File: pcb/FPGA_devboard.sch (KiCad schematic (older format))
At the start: 0 parts

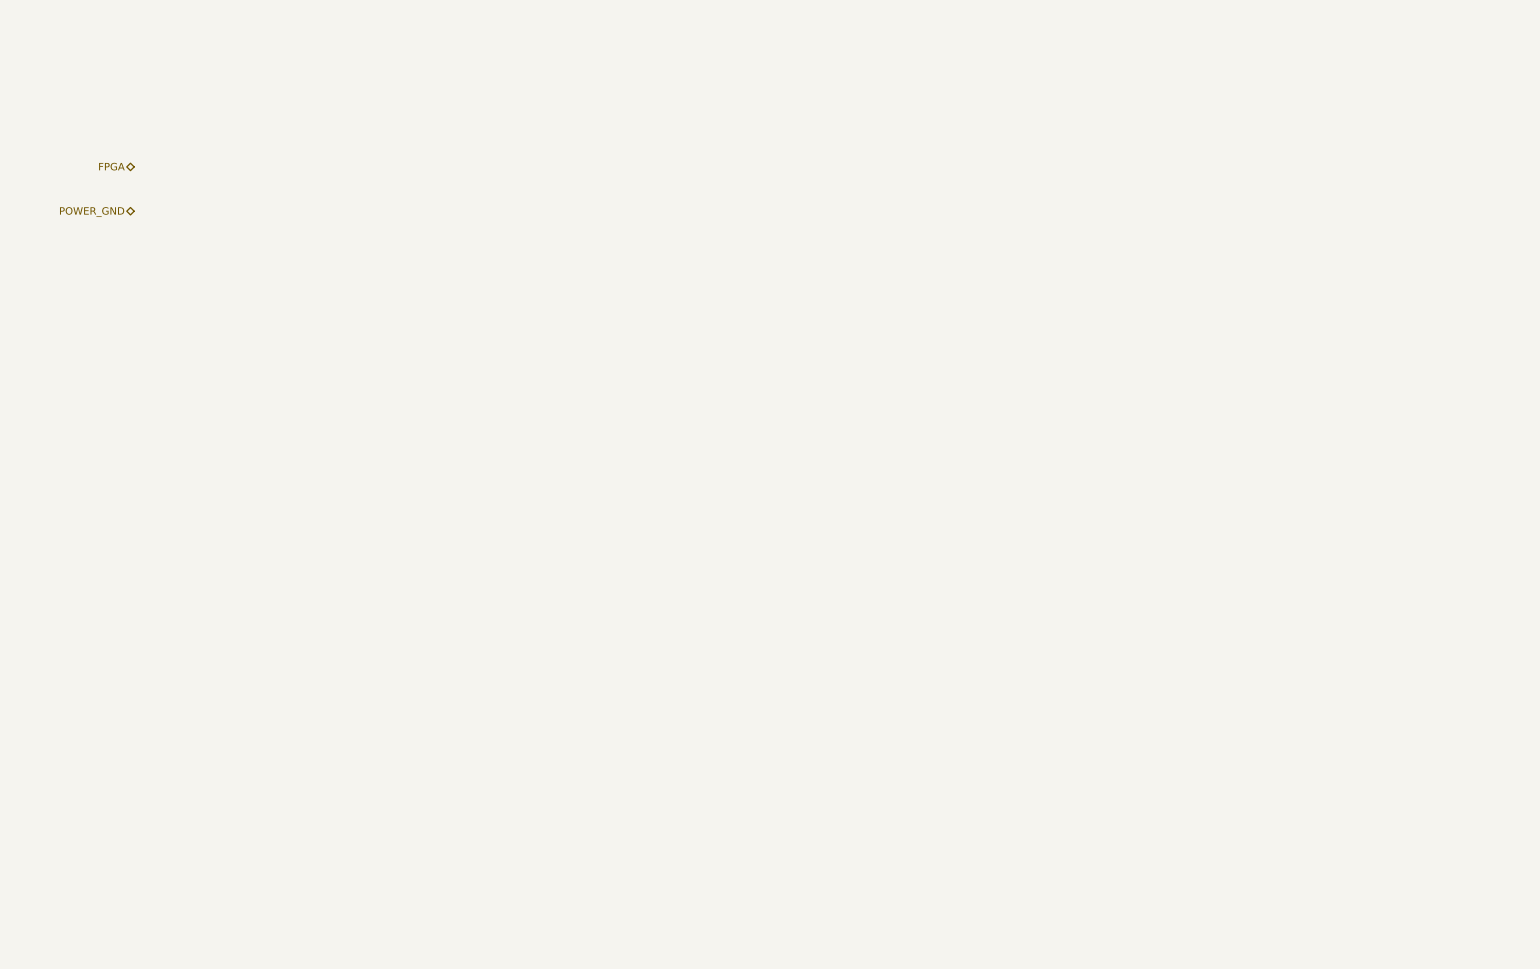
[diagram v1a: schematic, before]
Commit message: AC7020 schlib and sch list updated
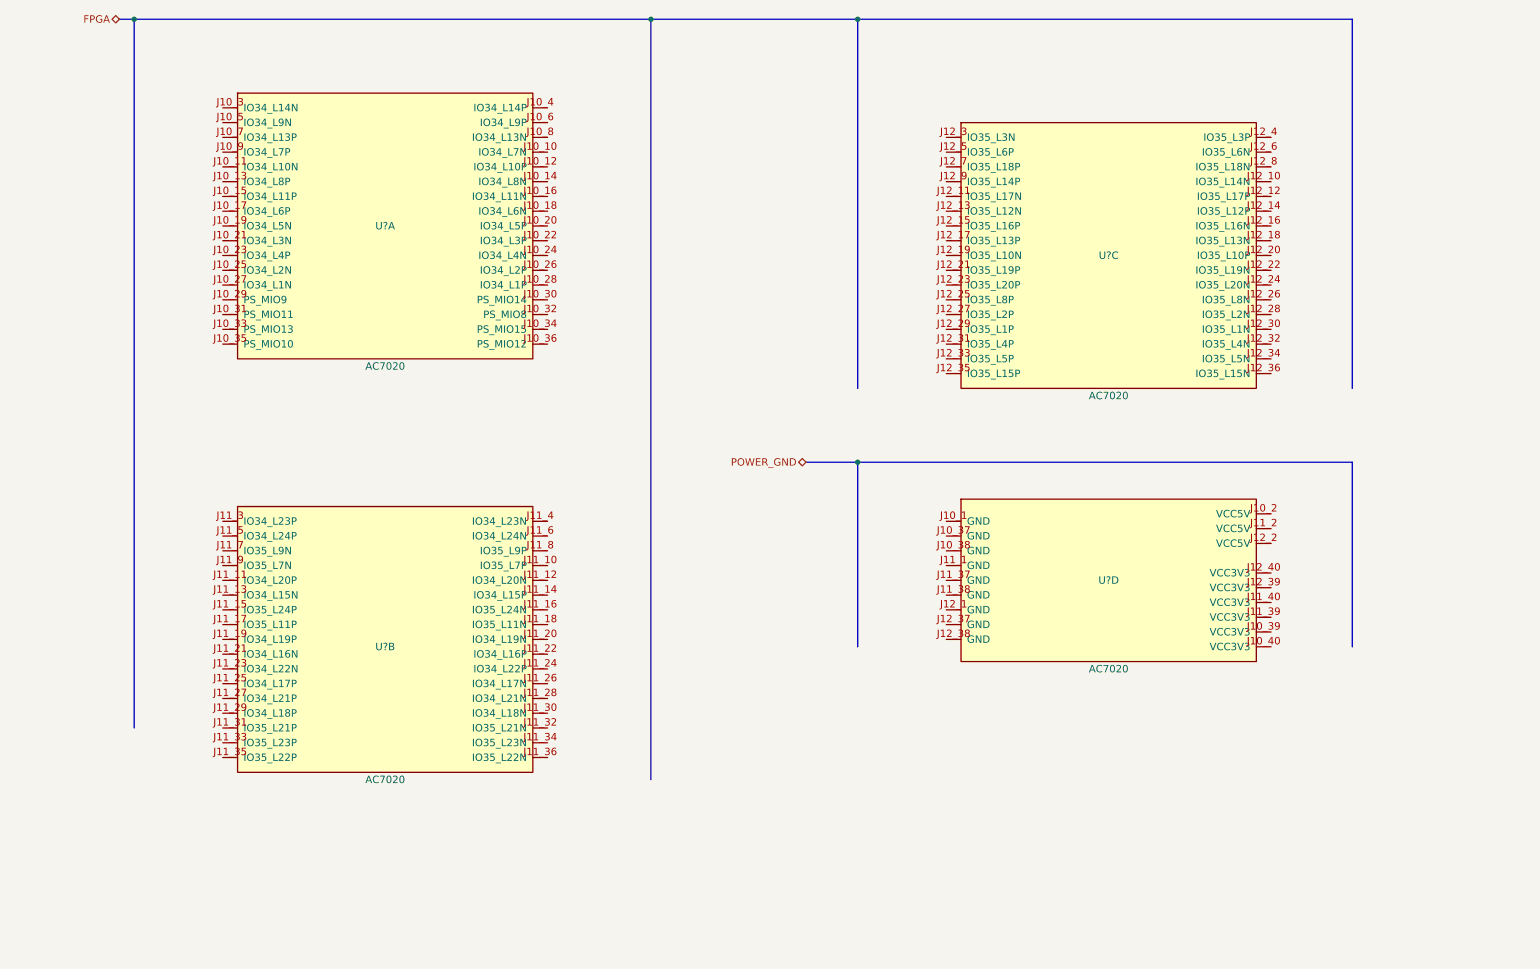
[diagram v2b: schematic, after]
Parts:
- added U? (x4): AC7020, symbol WM1200:AC7020
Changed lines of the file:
@@
 Comment4 ""
 $EndDescr
-Text HLabel 1500 2000 0    50   BiDi ~ 0
+Text HLabel 1400 1000 0    50   BiDi ~ 0
 FPGA
-Text HLabel 1500 2300 0    50   BiDi ~ 0
+Text HLabel 6050 4000 0    50   BiDi ~ 0
 POWER_GND
+$Comp
+L WM1200:AC7020 U?
+U 1 1 5EB9A3F4
+P 3200 3300
+F 0 "U?" H 3200 4200 50  0000 C CNN
+F 1 "AC7020" H 3200 3250 50  0000 C CNN
+F 2 "" H 3200 3300 50  0001 C CNN
+F 3 "" H 3200 3300 50  0001 C CNN
+	1    3200 3300
+	1    0    0    -1
+$EndComp
+$Comp
+L WM1200:AC7020 U?
+U 2 1 5EBA0B64
+P 3200 6100
+F 0 "U?" H 3200 6950 50  0000 C CNN
+F 1 "AC7020" H 3200 6050 50  0000 C CNN
+F 2 "" H 3200 6100 50  0001 C CNN
+F 3 "" H 3200 6100 50  0001 C CNN
+	2    3200 6100
+	1    0    0    -1
+$EndComp
+$Comp
+L WM1200:AC7020 U?
+U 3 1 5EBA7395
+P 8100 3500
+F 0 "U?" H 8100 4400 50  0000 C CNN
+F 1 "AC7020" H 8100 3450 50  0000 C CNN
+F 2 "" H 8100 3500 50  0001 C CNN
+F 3 "" H 8100 3500 50  0001 C CNN
+	3    8100 3500
+	1    0    0    -1
+$EndComp
+Wire Bus Line
+	1400 1000 1500 1000
+Wire Bus Line
+	1500 1000 1500 5800
+Wire Bus Line
+	1500 1000 5000 1000
+Wire Bus Line
+	5000 1000 5000 6150
+Connection ~ 1500 1000
+Wire Bus Line
+	5000 1000 6400 1000
+Wire Bus Line
+	6400 1000 6400 3500
+Connection ~ 5000 1000
+Wire Bus Line
+	6400 1000 9750 1000
+Wire Bus Line
+	9750 1000 9750 3500
+Connection ~ 6400 1000
+$Comp
+L WM1200:AC7020 U?
+U 4 1 5EBCCB73
+P 8100 5350
+F 0 "U?" H 8100 5900 50  0000 C CNN
+F 1 "AC7020" H 8100 5300 50  0000 C CNN
+F 2 "" H 8100 5350 50  0001 C CNN
+F 3 "" H 8100 5350 50  0001 C CNN
+	4    8100 5350
+	1    0    0    -1
+$EndComp
+Wire Bus Line
+	6050 4000 6400 4000
+Wire Bus Line
+	6400 4000 6400 5250
+Wire Bus Line
+	6400 4000 9750 4000
+Wire Bus Line
+	9750 4000 9750 5250
+Connection ~ 6400 4000
 $EndSCHEMATC

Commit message: Some work done on the whole project
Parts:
- gave numbers to parts that had none: 1
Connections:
- net FPGA_A17: now reaches X3.J10_10 (IO34_L7N)
- net FPGA_A4: now reaches X3.J10_11 (IO34_L10N)
- net FPGA_A18: now reaches X3.J10_12 (IO34_L10P)
- net FPGA_A5: now reaches X3.J10_13 (IO34_L8P)
- net FPGA_A19: now reaches X3.J10_14 (IO34_L8N)
- net FPGA_A6: now reaches X3.J10_15 (IO34_L11P)
- net FPGA_A20: now reaches X3.J10_16 (IO34_L11N)
- net FPGA_A7: now reaches X3.J10_17 (IO34_L6P)
- net FPGA_A21: now reaches X3.J10_18 (IO34_L6N)
- net FPGA_A8: now reaches X3.J10_19 (IO34_L5N)
- net FPGA_A22: now reaches X3.J10_20 (IO34_L5P)
- net FPGA_A9: now reaches X3.J10_21 (IO34_L3N)
- net FPGA_A23: now reaches X3.J10_22 (IO34_L3P)
- net FPGA_A10: now reaches X3.J10_23 (IO34_L4P)
- net A_BUFF_DIR: now reaches X3.J10_24 (IO34_L4N)
- net FPGA_A11: now reaches X3.J10_25 (IO34_L2N)
- net _A_BUFF_OE: now reaches X3.J10_26 (IO34_L2P)
- net FPGA_A12: now reaches X3.J10_27 (IO34_L1N)
- net FPGA_A0: now reaches X3.J10_3 (IO34_L14N)
- net FPGA_A13: now reaches X3.J10_4 (IO34_L14P)
- net FPGA_A1: now reaches X3.J10_5 (IO34_L9N)
- net FPGA_A14: now reaches X3.J10_6 (IO34_L9P)
- net FPGA_A2: now reaches X3.J10_7 (IO34_L13P)
- net FPGA_A15: now reaches X3.J10_8 (IO34_L13N)
- net FPGA_A3: now reaches X3.J10_9 (IO34_L7P)
- net FPGA_: now reaches X3.J11_10 (IO35_L7P)
- net FPGA_: now also X3.J11_11 (IO34_L20P), X3.J11_12 (IO34_L20N), X3.J11_13 (IO34_L15N), X3.J11_14 (IO34_L15P), X3.J11_15 (IO35_L24P), X3.J11_16 (IO35_L24N), X3.J11_17 (IO35_L11P), X3.J11_18 (IO35_L11N), X3.J11_19 (IO34_L19P), X3.J11_20 (IO34_L19N), X3.J11_21 (IO34_L16N), X3.J11_22 (IO34_L16P), X3.J11_23 (IO34_L22N), X3.J11_24 (IO34_L22P), X3.J11_25 (IO34_L17P), X3.J11_26 (IO34_L17N), X3.J11_27 (IO34_L21P), X3.J11_28 (IO34_L21N), X3.J11_29 (IO34_L18P), X3.J11_3 (IO34_L23P), X3.J11_30 (IO34_L18N), X3.J11_31 (IO35_L21P), X3.J11_32 (IO35_L21N), X3.J11_33 (IO35_L23P), X3.J11_34 (IO35_L23N), X3.J11_35 (IO35_L22P), X3.J11_36 (IO35_L22N), X3.J11_5 (IO34_L24P), X3.J11_7 (IO35_L9N), X3.J11_9 (IO35_L7N)
- net FPGA_AUD_PWM_L: now reaches X3.J11_4 (IO34_L23N)
- net FPGA_AUD_PWM_R: now reaches X3.J11_6 (IO34_L24N)
- net FPGA_AUD_SD: now reaches X3.J11_8 (IO35_L9P)
- net FPGA_D20: now reaches X3.J12_10 (IO35_L14N)
- net FPGA_D4: now reaches X3.J12_11 (IO35_L17N)
- net FPGA_D21: now reaches X3.J12_12 (IO35_L17P)
- net FPGA_D5: now reaches X3.J12_13 (IO35_L12N)
- net FPGA_D22: now reaches X3.J12_14 (IO35_L12P)
- net FPGA_D6: now reaches X3.J12_15 (IO35_L16P)
- net FPGA_D23: now reaches X3.J12_16 (IO35_L16N)
- net FPGA_D7: now reaches X3.J12_17 (IO35_L13P)
- net FPGA_D24: now reaches X3.J12_18 (IO35_L13N)
- net FPGA_D8: now reaches X3.J12_19 (IO35_L10N)
- net FPGA_D25: now reaches X3.J12_20 (IO35_L10P)
- net FPGA_D9: now reaches X3.J12_21 (IO35_L19P)
- net FPGA_D26: now reaches X3.J12_22 (IO35_L19N)
- net FPGA_D10: now reaches X3.J12_23 (IO35_L20P)
- net FPGA_D27: now reaches X3.J12_24 (IO35_L20N)
- net FPGA_D11: now reaches X3.J12_25 (IO35_L8P)
- net FPGA_D28: now reaches X3.J12_26 (IO35_L8N)
- net FPGA_D12: now reaches X3.J12_27 (IO35_L2P)
- net FPGA_D29: now reaches X3.J12_28 (IO35_L2N)
- net FPGA_D13: now reaches X3.J12_29 (IO35_L1P)
- net FPGA_D0: now reaches X3.J12_3 (IO35_L3N)
- net FPGA_D30: now reaches X3.J12_30 (IO35_L1N)
- net FPGA_D14: now reaches X3.J12_31 (IO35_L4P)
- net FPGA_D31: now reaches X3.J12_32 (IO35_L4N)
- net FPGA_D15: now reaches X3.J12_33 (IO35_L5P)
- net D_BUFF_DIR: now reaches X3.J12_34 (IO35_L5N)
- net FPGA_D16: now reaches X3.J12_35 (IO35_L15P)
- net _D_BUFF_OE: now reaches X3.J12_36 (IO35_L15N)
- net FPGA_D17: now reaches X3.J12_4 (IO35_L3P)
- net FPGA_D1: now reaches X3.J12_5 (IO35_L6P)
- net FPGA_D18: now reaches X3.J12_6 (IO35_L6N)
- net FPGA_D2: now reaches X3.J12_7 (IO35_L18P)
- net FPGA_D19: now reaches X3.J12_8 (IO35_L18N)
- net FPGA_D3: now reaches X3.J12_9 (IO35_L14P)
- net GND: now reaches X3.J10_1 (GND)
- net GND: now also X3.J10_37 (GND), X3.J10_38 (GND), X3.J11_1 (GND), X3.J11_37 (GND), X3.J11_38 (GND), X3.J12_1 (GND), X3.J12_37 (GND), X3.J12_38 (GND)
- net FPGA_VCC5V: now reaches X3.J10_2 (VCC5V)
- net FPGA_VCC5V: now also X3.J11_2 (VCC5V), X3.J12_2 (VCC5V)
- net FPGA_VCC3V3: now reaches X3.J10_39 (VCC3V3)
- net FPGA_VCC3V3: now also X3.J10_40 (VCC3V3), X3.J11_39 (VCC3V3), X3.J11_40 (VCC3V3), X3.J12_39 (VCC3V3), X3.J12_40 (VCC3V3)
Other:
- note added: "Addr lines"
- note added: "Data lines"
- moved on the sheet: X3C, X3D

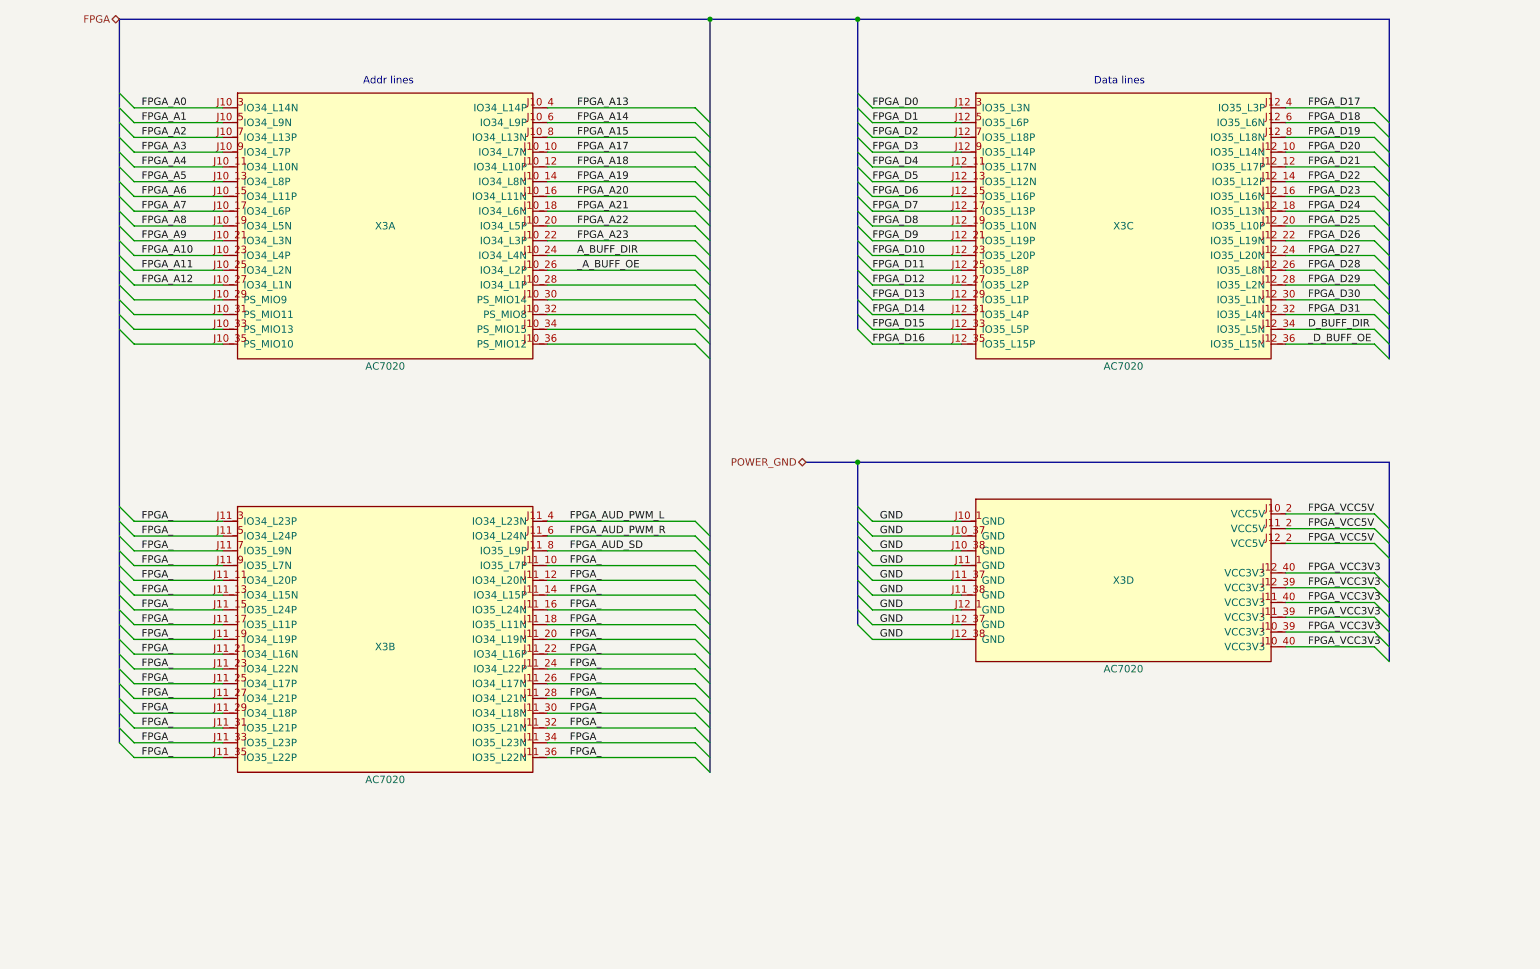
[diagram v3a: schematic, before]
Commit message: ok, we are using global labels now
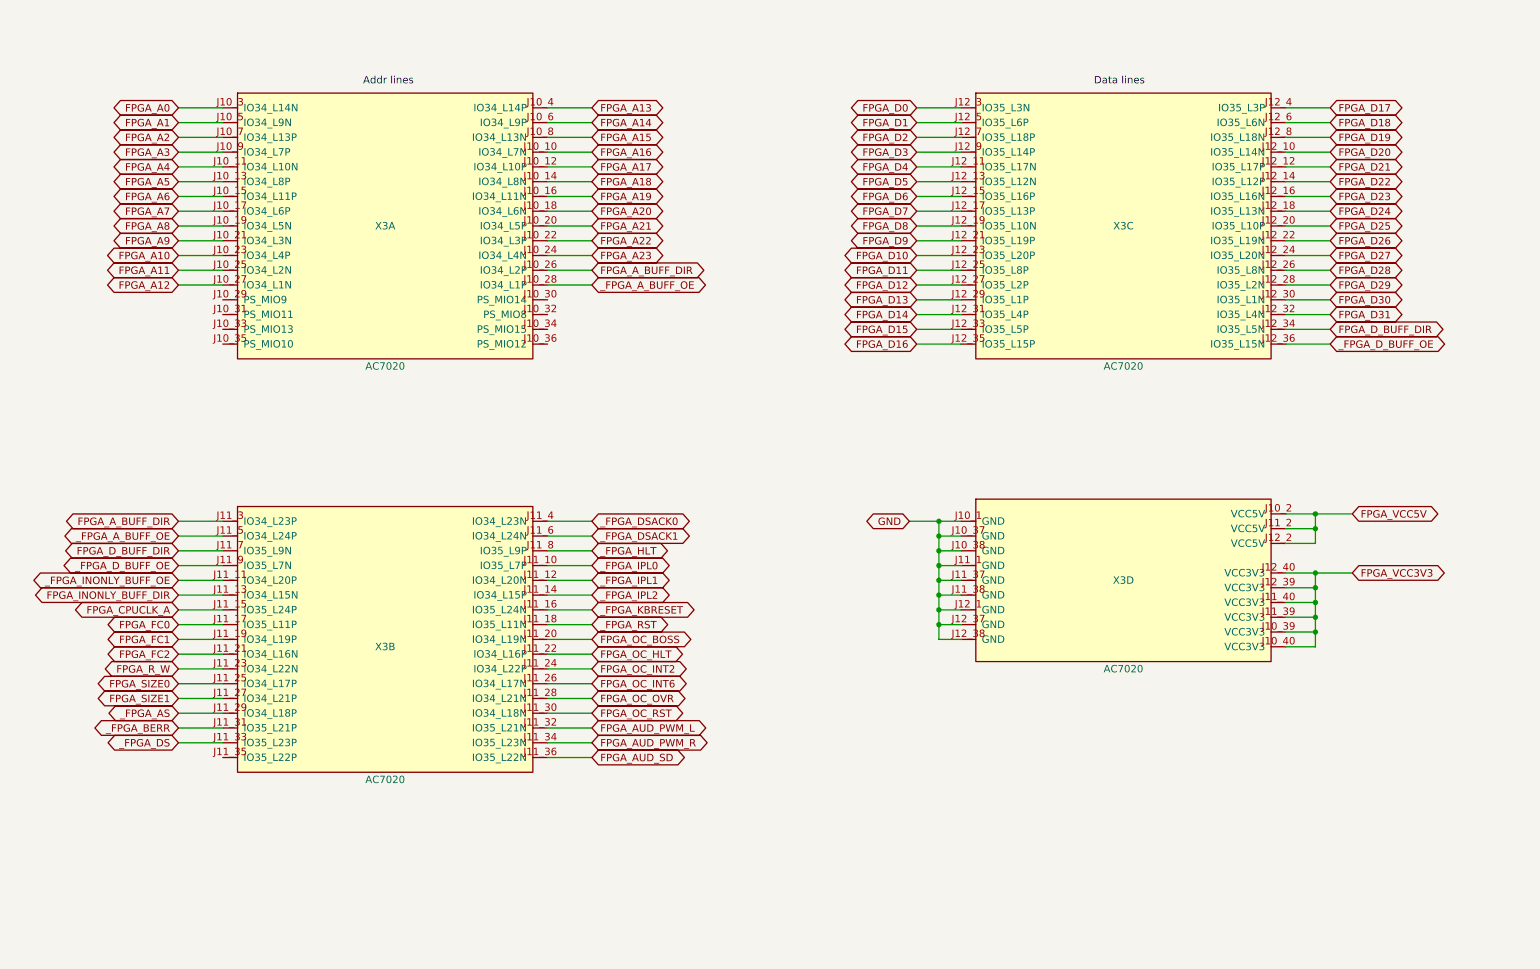
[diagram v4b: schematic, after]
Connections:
- net A_BUFF_DIR is gone; now on net FPGA_A23: X3.J10_24 (IO34_L4N)
- net FPGA_A17: now also X3.J10_12 (IO34_L10P); no longer X3.J10_10 (IO34_L7N)
- net FPGA_A18: now also X3.J10_14 (IO34_L8N); no longer X3.J10_12 (IO34_L10P)
- net FPGA_A19: now also X3.J10_16 (IO34_L11N); no longer X3.J10_14 (IO34_L8N)
- net FPGA_A20: now also X3.J10_18 (IO34_L6N); no longer X3.J10_16 (IO34_L11N)
- net FPGA_A21: now also X3.J10_20 (IO34_L5P); no longer X3.J10_18 (IO34_L6N)
- net FPGA_A22: now also X3.J10_22 (IO34_L3P); no longer X3.J10_20 (IO34_L5P)
- net FPGA_A23: no longer X3.J10_22 (IO34_L3P)
- net FPGA_AUD_PWM_L: now also X3.J11_32 (IO35_L21N); no longer X3.J11_4 (IO34_L23N)
- net FPGA_AUD_PWM_R: now also X3.J11_34 (IO35_L23N); no longer X3.J11_6 (IO34_L24N)
- net FPGA_AUD_SD: now also X3.J11_36 (IO35_L22N); no longer X3.J11_8 (IO35_L9P)
- net _FPGA_A_BUFF_OE: now reaches X3.J10_28 (IO34_L1P)
- net _FPGA_A_BUFF_OE: now also X3.J11_5 (IO34_L24P)
- net D_BUFF_DIR renamed FPGA_D_BUFF_DIR
- net FPGA_D_BUFF_DIR: now also X3.J11_7 (IO35_L9N)
- removed net FPGA_: X3.J11_10 (IO35_L7P), X3.J11_11 (IO34_L20P), X3.J11_12 (IO34_L20N), X3.J11_13 (IO34_L15N), X3.J11_14 (IO34_L15P), X3.J11_15 (IO35_L24P), X3.J11_16 (IO35_L24N), X3.J11_17 (IO35_L11P), X3.J11_18 (IO35_L11N), X3.J11_19 (IO34_L19P), X3.J11_20 (IO34_L19N), X3.J11_21 (IO34_L16N), X3.J11_22 (IO34_L16P), X3.J11_23 (IO34_L22N), X3.J11_24 (IO34_L22P), X3.J11_25 (IO34_L17P), X3.J11_26 (IO34_L17N), X3.J11_27 (IO34_L21P), X3.J11_28 (IO34_L21N), X3.J11_29 (IO34_L18P), X3.J11_3 (IO34_L23P), X3.J11_30 (IO34_L18N), X3.J11_31 (IO35_L21P), X3.J11_32 (IO35_L21N), X3.J11_33 (IO35_L23P), X3.J11_34 (IO35_L23N), X3.J11_35 (IO35_L22P), X3.J11_36 (IO35_L22N), X3.J11_5 (IO34_L24P), X3.J11_7 (IO35_L9N), X3.J11_9 (IO35_L7N)
- net _A_BUFF_OE renamed FPGA_A_BUFF_DIR
- net FPGA_A_BUFF_DIR: now also X3.J11_3 (IO34_L23P)
- net _D_BUFF_OE renamed _FPGA_D_BUFF_OE
- net _FPGA_D_BUFF_OE: now also X3.J11_9 (IO35_L7N)
- new net FPGA_A16: X3.J10_10 (IO34_L7N)
- new net FPGA_CPUCLK_A: X3.J11_15 (IO35_L24P)
- new net FPGA_FC0: X3.J11_17 (IO35_L11P)
- new net FPGA_FC1: X3.J11_19 (IO34_L19P)
- new net FPGA_FC2: X3.J11_21 (IO34_L16N)
- new net FPGA_INONLY_BUFF_DIR: X3.J11_13 (IO34_L15N)
- new net FPGA_OC_BOSS: X3.J11_20 (IO34_L19N)
- new net FPGA_OC_HLT: X3.J11_22 (IO34_L16P)
- new net FPGA_OC_INT2: X3.J11_24 (IO34_L22P)
- new net FPGA_OC_INT6: X3.J11_26 (IO34_L17N)
- new net FPGA_OC_OVR: X3.J11_28 (IO34_L21N)
- new net FPGA_OC_RST: X3.J11_30 (IO34_L18N)
- new net FPGA_R_W: X3.J11_23 (IO34_L22N)
- new net FPGA_SIZE0: X3.J11_25 (IO34_L17P)
- new net FPGA_SIZE1: X3.J11_27 (IO34_L21P)
- new net _FPGA_AS: X3.J11_29 (IO34_L18P)
- new net _FPGA_BERR: X3.J11_31 (IO35_L21P)
- new net _FPGA_DS: X3.J11_33 (IO35_L23P)
- new net _FPGA_DSACK0: X3.J11_4 (IO34_L23N)
- new net _FPGA_DSACK1: X3.J11_6 (IO34_L24N)
- new net _FPGA_HLT: X3.J11_8 (IO35_L9P)
- new net _FPGA_INONLY_BUFF_OE: X3.J11_11 (IO34_L20P)
- new net _FPGA_IPL0: X3.J11_10 (IO35_L7P)
- new net _FPGA_IPL1: X3.J11_12 (IO34_L20N)
- new net _FPGA_IPL2: X3.J11_14 (IO34_L15P)
- new net _FPGA_KBRESET: X3.J11_16 (IO35_L24N)
- new net _FPGA_RST: X3.J11_18 (IO35_L11N)
